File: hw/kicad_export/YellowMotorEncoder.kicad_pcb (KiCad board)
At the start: 2 copper layers, 35 x 22.2 mm, 22 parts, among them P1 M1

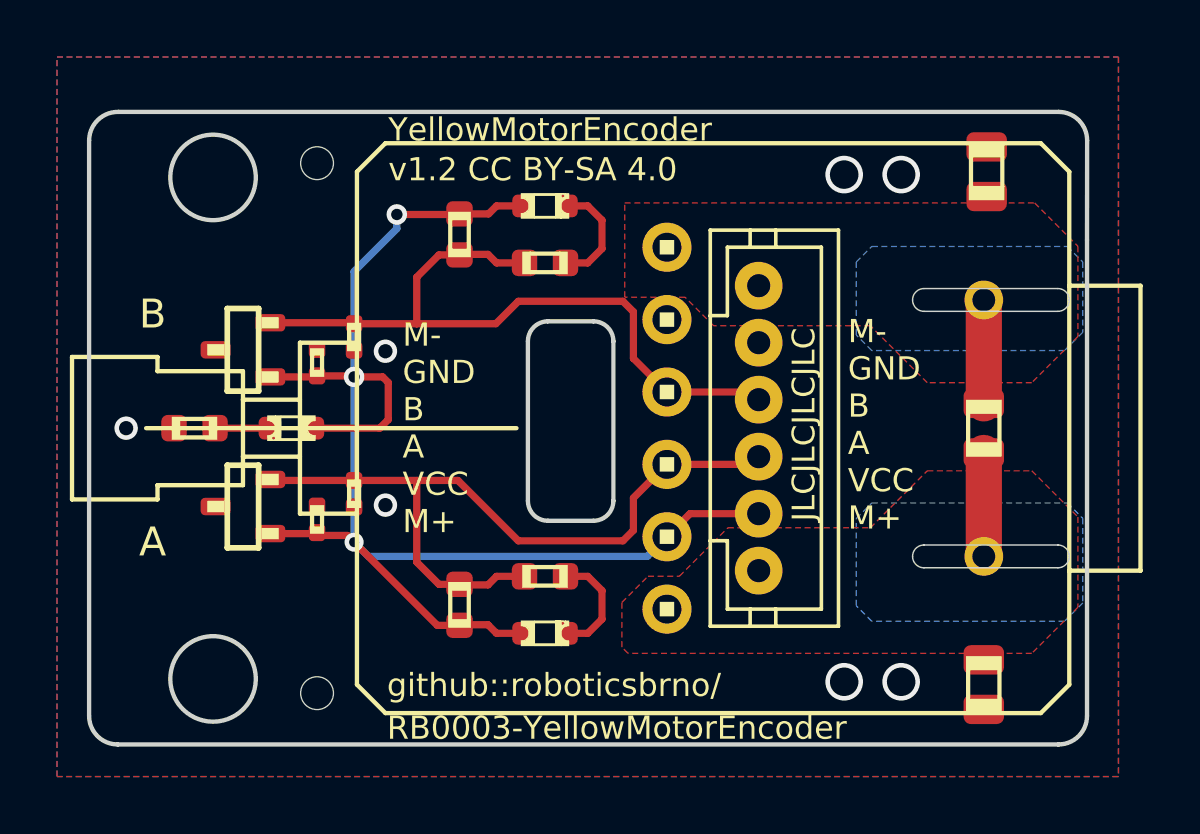
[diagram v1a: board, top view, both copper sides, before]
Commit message: Update shape of motor's slotted holes in Kicad exported board
- change the shape from circle to oval as this feature is supported in Kicad
- fix missing capacitor in KiKit export - move their label inside PCB border
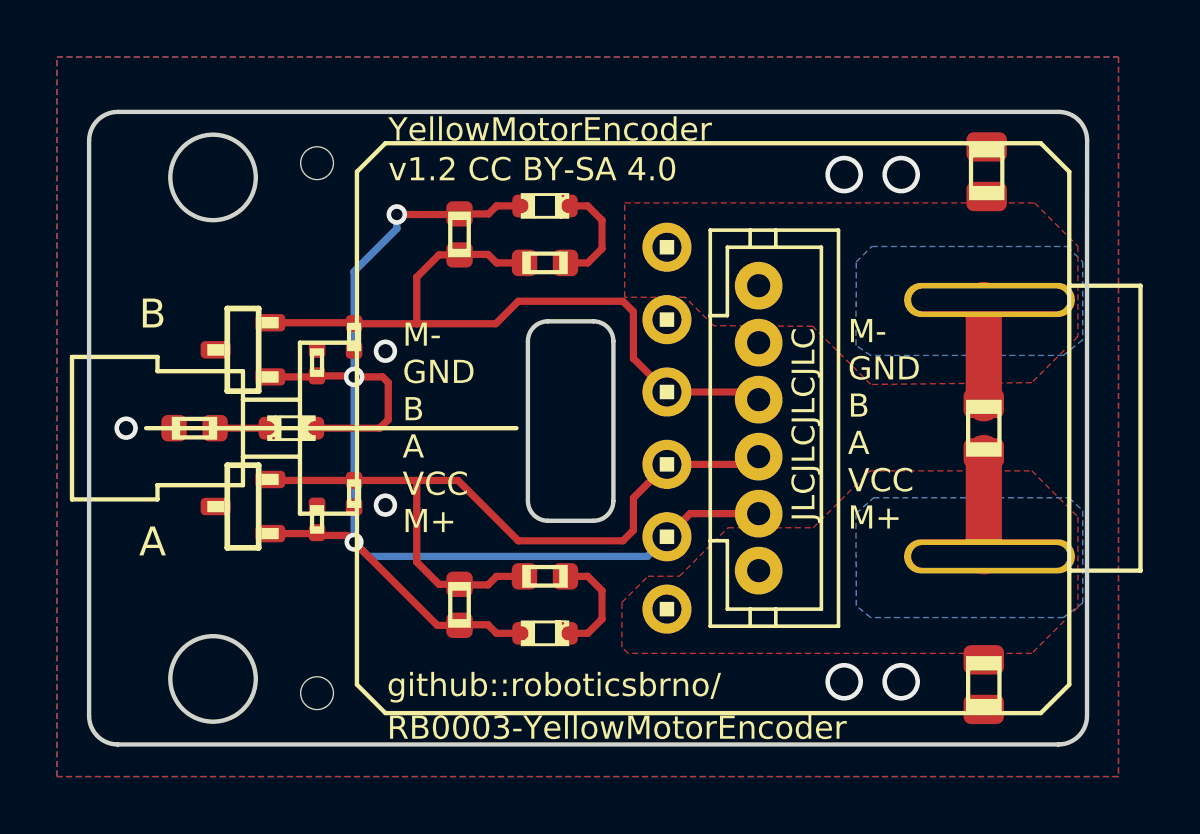
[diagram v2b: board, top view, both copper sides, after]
